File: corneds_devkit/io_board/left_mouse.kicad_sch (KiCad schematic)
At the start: 0 parts

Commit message: finished mouse and key boards
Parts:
- added D85: APA-106-F5, LED_THT:LED_D5.0mm-4_RGB, symbol LED:APA-106-F5
- added D86: 1N4148W, Diode_SMD:D_SOD-123, symbol Diode:1N4148W
- added SW43: SW_Push, symbol Switch:SW_Push
- added U1: COM-09426, symbol entropy:COM-09426
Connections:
- new net: D86.2 (A), SW43.2
- new net GNDL: D85.2 (GND), U1.4 (GND)
- new net VDDL: D85.3 (VDD), SW43.1
- new net VJOYL: U1.2 (VDD)
- new net key_lclick: D86.1 (K)
- new net lclick_led_di: D85.4 (DI)
- new net scroll_x: U1.1 (x-axis)
- new net scroll_y: U1.3 (y-axis)
- no-connect marks 1 -> 0

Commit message: finished schematic for io board
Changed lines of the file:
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@@
+		)
+	)
+	(global_label "GNDL"
+		(shape input)
+		(at 161.29 81.28 270)
+		(fields_autoplaced yes)
+		(effects
+			(font
+				(size 1.27 1.27)
+			)
+			(justify right)
+		)
+		(property "Intersheetrefs" "${INTERSHEET_REFS}"
+			(at 161.29 89.1638 90)
+			(effects
+				(font
+					(size 1.27 1.27)
+				)
+				(justify right)
+				(hide yes)
+			)
 		)
 	)
@@
 		(property "Intersheetrefs" "${INTERSHEET_REFS}"
 			(at 136.0932 60.96 0)
+			(effects
+				(font
+					(size 1.27 1.27)
+				)
+				(justify left)
+				(hide yes)
+			)
+		)
+	)
+	(global_label "VJOYL"
+		(shape input)
+		(at 111.76 50.8 90)
+		(fields_autoplaced yes)
+		(effects
+			(font
+				(size 1.27 1.27)
+			)
+			(justify left)
+		)
+		(property "Intersheetrefs" "${INTERSHEET_REFS}"
+			(at 111.76 42.3114 90)
+			(effects
+				(font
+					(size 1.27 1.27)
+				)
+				(justify left)
+				(hide yes)
+			)
+		)
+	)
+	(global_label "VDDL"
+		(shape input)
+		(at 152.4 50.8 90)
+		(fields_autoplaced yes)
+		(effects
+			(font
+				(size 1.27 1.27)
+			)
+			(justify left)
+		)
+		(property "Intersheetrefs" "${INTERSHEET_REFS}"
+			(at 152.4 43.1581 90)
 			(effects
 				(font
@@
 	)
 	(symbol
-		(lib_id "power:VDD")
-		(at 111.76 50.8 0)
-		(unit 1)
-		(exclude_from_sim no)
-		(in_bom yes)
-		(on_board yes)
-		(dnp no)
-		(fields_autoplaced yes)
-		(property "Reference" "#PWR07"
-			(at 111.76 54.61 0)
-			(effects
-				(font
-					(size 1.27 1.27)
-				)
-				(hide yes)
-			)
-		)
-		(property "Value" "VJOYL"
-			(at 111.76 45.72 0)
-			(effects
-				(font
-					(size 1.27 1.27)
-				)
-			)
-		)
-		(property "Footprint" ""
-			(at 111.76 50.8 0)
-			(effects
-				(font
-					(size 1.27 1.27)
-				)
-				(hide yes)
-			)
-		)
-		(property "Datasheet" ""
-			(at 111.76 50.8 0)
-			(effects
-				(font
-					(size 1.27 1.27)
-				)
-				(hide yes)
-			)
-		)
-		(property "Description" "Power symbol creates a global label with name \"VDD\""
-			(at 111.76 50.8 0)
-			(effects
-				(font
-					(size 1.27 1.27)
-				)
-				(hide yes)
-			)
-		)
-		(pin "1"
-		)
-		(instances
-			(project "io_board"
-				(path "/244b6d6b-132d-4d50-ae86-e41103b29008/f7f8749d-d618-4fa3-a34a-defbc416e54b"
-					(reference "#PWR07")
-					(unit 1)
-				)
-			)
-		)
-	)
-	(symbol
 		(lib_id "Switch:SW_Push")
 		(at 161.29 60.96 0)
@@
 	)
 	(symbol
-		(lib_id "power:VDD")
-		(at 152.4 50.8 0)
-		(unit 1)
-		(exclude_from_sim no)
-		(in_bom yes)
-		(on_board yes)
-		(dnp no)
-		(fields_autoplaced yes)
-		(property "Reference" "#PWR05"
-			(at 152.4 54.61 0)
-			(effects
-				(font
-					(size 1.27 1.27)
-				)
-				(hide yes)
-			)
-		)
-		(property "Value" "VDDL"
-			(at 152.4 45.72 0)
-			(effects
-				(font
-					(size 1.27 1.27)
-				)
-			)
-		)
-		(property "Footprint" ""
-			(at 152.4 50.8 0)
-			(effects
-				(font
-					(size 1.27 1.27)
-				)
-				(hide yes)
-			)
-		)
-		(property "Datasheet" ""
-			(at 152.4 50.8 0)
-			(effects
-				(font
-					(size 1.27 1.27)
-				)
-				(hide yes)
-			)
-		)
-		(property "Description" "Power symbol creates a global label with name \"VDD\""
-			(at 152.4 50.8 0)
-			(effects
-				(font
-					(size 1.27 1.27)
-				)
-				(hide yes)
-			)
-		)
-		(pin "1"
-		)
-		(instances
-			(project "io_board"
-				(path "/244b6d6b-132d-4d50-ae86-e41103b29008/f7f8749d-d618-4fa3-a34a-defbc416e54b"
-					(reference "#PWR05")
-					(unit 1)
-				)
-			)
-		)
-	)
-	(symbol
 		(lib_id "Diode:1N4148W")
 		(at 171.45 60.96 180)
@@
 					(unit 1)
 				)
-			)
-		)
-	)
-	(symbol
-		(lib_id "power:GND")
-		(at 161.29 81.28 0)
-		(unit 1)
-		(exclude_from_sim no)
-		(in_bom yes)
-		(on_board yes)
-		(dnp no)
-		(fields_autoplaced yes)
-		(property "Reference" "#PWR06"
-			(at 161.29 87.63 0)
-			(effects
-				(font
-					(size 1.27 1.27)
-				)
-				(hide yes)
-			)
-		)
-		(property "Value" "GNDL"
-			(at 161.29 86.36 0)
-			(effects
-				(font
-					(size 1.27 1.27)
-				)
-			)
-		)
-		(property "Footprint" ""
-			(at 161.29 81.28 0)
-			(effects
-				(font
-					(size 1.27 1.27)
-				)
-				(hide yes)
-			)
-		)
-		(property "Datasheet" ""
-			(at 161.29 81.28 0)
-			(effects
-				(font
-					(size 1.27 1.27)
-				)
-				(hide yes)
-			)
-		)
-		(property "Description" "Power symbol creates a global label with name \"GND\" , ground"
-			(at 161.29 81.28 0)
-			(effects
-				(font
-					(size 1.27 1.27)
-				)
-				(hide yes)
-			)
-		)
-		(pin "1"
-		)
-		(instances
-			(project "io_board"
-				(path "/244b6d6b-132d-4d50-ae86-e41103b29008/f7f8749d-d618-4fa3-a34a-defbc416e54b"
-					(reference "#PWR06")
-					(unit 1)
-				)

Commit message: re-routed io board with keypad IC
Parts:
- removed D86: 1N4148W, Diode_SMD:D_SOD-123, symbol Diode:1N4148W
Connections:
- net VDDL: no longer SW43.1
- net ROW3L: now reaches SW43.2
- new net COL2L: SW43.1
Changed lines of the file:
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@@
 		(color 0 0 0 0)
 	)
-	(junction
-		(at 152.4 60.96)
-		(diameter 0)
-		(color 0 0 0 0)
-	)
 	(wire
 		(pts
@@
 	(wire
 		(pts
-			(xy 152.4 60.96) (xy 152.4 64.77)
+			(xy 147.32 58.42) (xy 147.32 64.77)
 		)
 		(stroke
@@
 	(wire
 		(pts
-			(xy 175.26 60.96) (xy 177.8 60.96)
-		)
-		(stroke
-			(width 0)
-			(type default)
-		)
-	)
-	(wire
-		(pts
-			(xy 156.21 60.96) (xy 152.4 60.96)
+			(xy 153.67 60.96) (xy 153.67 58.42)
 		)
 		(stroke
@@
 	(wire
 		(pts
-			(xy 161.29 64.77) (xy 152.4 64.77)
+			(xy 161.29 64.77) (xy 147.32 64.77)
 		)
 		(stroke
@@
 	(wire
 		(pts
-			(xy 152.4 50.8) (xy 152.4 60.96)
-		)
-		(stroke
-			(width 0)
-			(type default)
-		)
-	)
-	(wire
-		(pts
-			(xy 166.37 60.96) (xy 167.64 60.96)
+			(xy 166.37 60.96) (xy 171.45 60.96)
 		)
 		(stroke
@@
 		)
 	)
+	(wire
+		(pts
+			(xy 156.21 60.96) (xy 153.67 60.96)
+		)
+		(stroke
+			(width 0)
+			(type default)
+		)
+	)
 	(global_label "GNDL"
 		(shape input)
@@
 		)
 	)
+	(global_label "COL2L"
+		(shape input)
+		(at 153.67 58.42 90)
+		(fields_autoplaced yes)
+		(effects
+			(font
+				(size 1.27 1.27)
+			)
+			(justify left)
+		)
+		(property "Intersheetrefs" "${INTERSHEET_REFS}"
+			(at 153.67 49.5686 90)
+			(effects
+				(font
+					(size 1.27 1.27)
+				)
+				(justify left)
+				(hide yes)
+			)
+		)
+	)
+	(global_label "ROW3L"
+		(shape input)
+		(at 171.45 60.96 0)
+		(fields_autoplaced yes)
+		(effects
+			(font
+				(size 1.27 1.27)
+			)
+			(justify left)
+		)
+		(property "Intersheetrefs" "${INTERSHEET_REFS}"
+			(at 180.7247 60.96 0)
+			(effects
+				(font
+					(size 1.27 1.27)
+				)
+				(justify left)
+				(hide yes)
+			)
+		)
+	)
 	(global_label "scroll_x"
 		(shape input)
@@
 	(global_label "VDDL"
 		(shape input)
-		(at 152.4 50.8 90)
-		(fields_autoplaced yes)
-		(effects
-			(font
-				(size 1.27 1.27)
-			)
-			(justify left)
-		)
-		(property "Intersheetrefs" "${INTERSHEET_REFS}"
-			(at 152.4 43.1581 90)
+		(at 147.32 58.42 90)
+		(fields_autoplaced yes)
+		(effects
+			(font
+				(size 1.27 1.27)
+			)
+			(justify left)
+		)
+		(property "Intersheetrefs" "${INTERSHEET_REFS}"
+			(at 147.32 50.7781 90)
 			(effects
 				(font
@@
 				)
 				(justify right)
-				(hide yes)
-			)
-		)
-	)
-	(global_label "key_lclick"
-		(shape input)
-		(at 177.8 60.96 0)
-		(fields_autoplaced yes)
-		(effects
-			(font
-				(size 1.27 1.27)
-			)
-			(justify left)
-		)
-		(property "Intersheetrefs" "${INTERSHEET_REFS}"
-			(at 189.9776 60.96 0)
-			(effects
-				(font
-					(size 1.27 1.27)
-				)
-				(justify left)
 				(hide yes)
 			)
@@
 					(unit 1)
 				)
-			)
-		)
-	)
-	(symbol
-		(lib_id "Diode:1N4148W")
-		(at 171.45 60.96 180)
-		(unit 1)
-		(exclude_from_sim no)
-		(in_bom yes)
-		(on_board yes)
-		(dnp no)
-		(fields_autoplaced yes)
-		(property "Reference" "D86"
-			(at 171.45 54.61 0)
-			(effects
-				(font
-					(size 1.27 1.27)
-				)
-			)
-		)
-		(property "Value" "1N4148W"
-			(at 171.45 57.15 0)
-			(effects
-				(font
-					(size 1.27 1.27)
-				)
-			)
-		)
-		(property "Footprint" "Diode_SMD:D_SOD-123"
-			(at 171.45 56.515 0)
-			(effects
-				(font
-					(size 1.27 1.27)
-				)
-				(hide yes)
-			)
-		)
-		(property "Datasheet" "https://www.vishay.com/docs/85748/1n4148w.pdf"
-			(at 171.45 60.96 0)
-			(effects
-				(font
-					(size 1.27 1.27)
-				)
-				(hide yes)
-			)
-		)
-		(property "Description" "75V 0.15A Fast Switching Diode, SOD-123"
-			(at 171.45 60.96 0)
-			(effects
-				(font
-					(size 1.27 1.27)
-				)
-				(hide yes)
-			)
-		)
-		(pin "1"
-		)
-		(pin "2"
-		)
-		(instances
-			(project "io_board"
-				(path "/244b6d6b-132d-4d50-ae86-e41103b29008/f7f8749d-d618-4fa3-a34a-defbc416e54b"
-					(reference "D86")
-					(unit 1)
-				)

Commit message: added switch footprint, io sch, and keypad IC footprint. Need to find new LEDs and make joystick footprint
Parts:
- SW43: footprint (none) -> key-switches:SW_Gateron_LowProfile_HotSwap_THT
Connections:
- net VDDL renamed VDD_3V3L
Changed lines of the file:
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@@
 		)
 	)
-	(global_label "VDDL"
+	(global_label "VDD_3V3L"
 		(shape input)
 		(at 147.32 58.42 90)
@@
 		)
 		(property "Intersheetrefs" "${INTERSHEET_REFS}"
-			(at 147.32 50.7781 90)
+			(at 147.32 46.3029 90)
 			(effects
 				(font
@@
 			)
 		)
-		(property "Footprint" ""
+		(property "Footprint" "key-switches:SW_Gateron_LowProfile_HotSwap_THT"
 			(at 161.29 55.88 0)
 			(effects

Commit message: io sch done. Need to route
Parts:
- D85: value APA-106-F5 -> SK68XX-SIDE; footprint LED_THT:LED_D5.0mm-4_RGB -> entropy:SK68XX-SIDE
- U1: footprint (none) -> entropy:COM-09426
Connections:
- net VDD_3V3L renamed VDD_5VL
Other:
- moved on the sheet: U1
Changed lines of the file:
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@@
 	(wire
 		(pts
-			(xy 123.19 60.96) (xy 125.73 60.96)
-		)
-		(stroke
-			(width 0)
-			(type default)
-		)
-	)
-	(wire
-		(pts
-			(xy 123.19 66.04) (xy 125.73 66.04)
+			(xy 124.46 60.96) (xy 127 60.96)
+		)
+		(stroke
+			(width 0)
+			(type default)
+		)
+	)
+	(wire
+		(pts
+			(xy 124.46 66.04) (xy 127 66.04)
 		)
 		(stroke
@@
 	(global_label "scroll_x"
 		(shape input)
-		(at 125.73 60.96 0)
-		(fields_autoplaced yes)
-		(effects
-			(font
-				(size 1.27 1.27)
-			)
-			(justify left)
-		)
-		(property "Intersheetrefs" "${INTERSHEET_REFS}"
-			(at 136.0932 60.96 0)
+		(at 127 60.96 0)
+		(fields_autoplaced yes)
+		(effects
+			(font
+				(size 1.27 1.27)
+			)
+			(justify left)
+		)
+		(property "Intersheetrefs" "${INTERSHEET_REFS}"
+			(at 137.3632 60.96 0)
 			(effects
 				(font
@@
 		)
 	)
-	(global_label "VDD_3V3L"
+	(global_label "VDD_5VL"
 		(shape input)
 		(at 147.32 58.42 90)
@@
 		)
 		(property "Intersheetrefs" "${INTERSHEET_REFS}"
-			(at 147.32 46.3029 90)
+			(at 147.32 47.5124 90)
 			(effects
 				(font
@@
 	(global_label "scroll_y"
 		(shape input)
-		(at 125.73 66.04 0)
-		(fields_autoplaced yes)
-		(effects
-			(font
-				(size 1.27 1.27)
-			)
-			(justify left)
-		)
-		(property "Intersheetrefs" "${INTERSHEET_REFS}"
-			(at 136.0327 66.04 0)
+		(at 127 66.04 0)
+		(fields_autoplaced yes)
+		(effects
+			(font
+				(size 1.27 1.27)
+			)
+			(justify left)
+		)
+		(property "Intersheetrefs" "${INTERSHEET_REFS}"
+			(at 137.3027 66.04 0)
 			(effects
 				(font
@@
 			)
 		)
-		(property "Value" "APA-106-F5"
+		(property "Value" "SK68XX-SIDE"
 			(at 173.99 66.0714 0)
 			(effects
@@
 			)
 		)
-		(property "Footprint" "LED_THT:LED_D5.0mm-4_RGB"
+		(property "Footprint" "entropy:SK68XX-SIDE"
 			(at 162.56 80.01 0)
 			(effects
@@
 			)
 		)
-		(property "Datasheet" "https://cdn.sparkfun.com/datasheets/Components/LED/COM-12877.pdf"
+		(property "Datasheet" "https://www.digikey.com/en/products/detail/adafruit-industries-llc/4691/13170955"
 			(at 163.83 81.915 0)
 			(effects
@@
 	(symbol
 		(lib_id "entropy:COM-09426")
-		(at 115.57 63.5 0)
+		(at 114.3 63.5 0)
 		(unit 1)
 		(exclude_from_sim no)
@@
 		(fields_autoplaced yes)
 		(property "Reference" "U1"
-			(at 107.95 62.2299 0)
+			(at 106.68 62.2299 0)
 			(effects
 				(font
@@
 		)
 		(property "Value" "COM-09426"
-			(at 107.95 64.7699 0)
+			(at 106.68 64.7699 0)
 			(effects
 				(font
@@
 			)
 		)
-		(property "Footprint" ""
-			(at 113.03 63.5 0)
+		(property "Footprint" "entropy:COM-09426"
+			(at 111.76 63.5 0)
 			(effects
 				(font
@@
 		)
 		(property "Datasheet" ""
-			(at 113.03 63.5 0)
+			(at 111.76 63.5 0)
 			(effects
 				(font
@@
 		)
 		(property "Description" "https://www.sparkfun.com/products/9426"
-			(at 113.03 63.5 0)
-			(effects
-				(font
+			(at 111.76 63.5 0)
+			(effects
+				(font

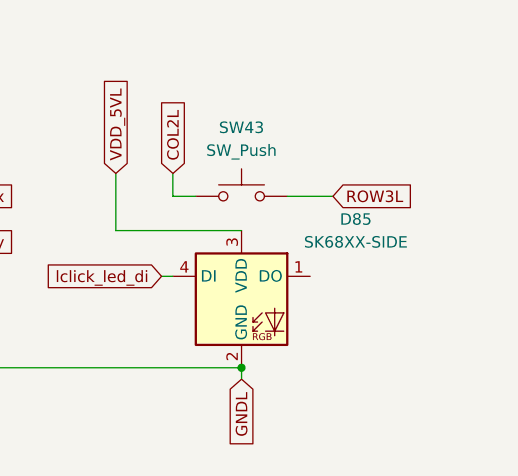
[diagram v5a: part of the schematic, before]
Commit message: routing left keys pcb
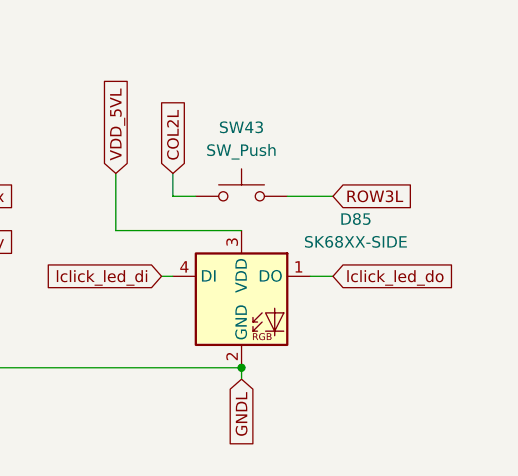
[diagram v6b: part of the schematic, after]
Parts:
- SW43: footprint key-switches:SW_Gateron_LowProfile_HotSwap_THT -> key-switches:SW_Gateron_LowProfile_HotSwap_PTH
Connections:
- net lclick_led_do: now reaches D85.1 (DO)
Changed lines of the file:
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@@
+	(wire
+		(pts
+			(xy 168.91 69.85) (xy 171.45 69.85)
+		)
+		(stroke
+			(width 0)
+			(type default)
+		)
+	)
 	(wire
 		(pts
@@
 				)
 				(justify right)
+				(hide yes)
+			)
+		)
+	)
+	(global_label "lclick_led_do"
+		(shape input)
+		(at 171.45 69.85 0)
+		(fields_autoplaced yes)
+		(effects
+			(font
+				(size 1.27 1.27)
+			)
+			(justify left)
+		)
+		(property "Intersheetrefs" "${INTERSHEET_REFS}"
+			(at 186.7117 69.85 0)
+			(effects
+				(font
+					(size 1.27 1.27)
+				)
+				(justify left)
 				(hide yes)
 			)
@@
 			)
 		)
-		(property "Footprint" "key-switches:SW_Gateron_LowProfile_HotSwap_THT"
+		(property "Footprint" "key-switches:SW_Gateron_LowProfile_HotSwap_PTH"
 			(at 161.29 55.88 0)
 			(effects
